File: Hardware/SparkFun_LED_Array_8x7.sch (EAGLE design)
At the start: 72 parts

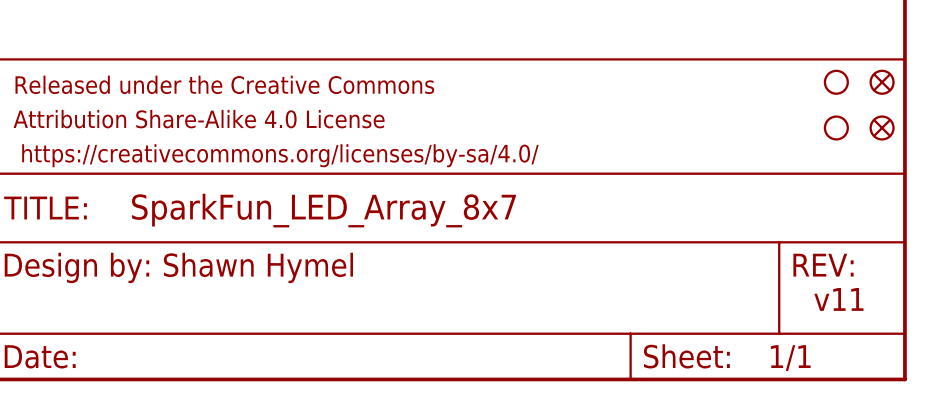
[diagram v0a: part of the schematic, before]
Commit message: Updated library to break up the page template and version number. Printed pdf of schematic.
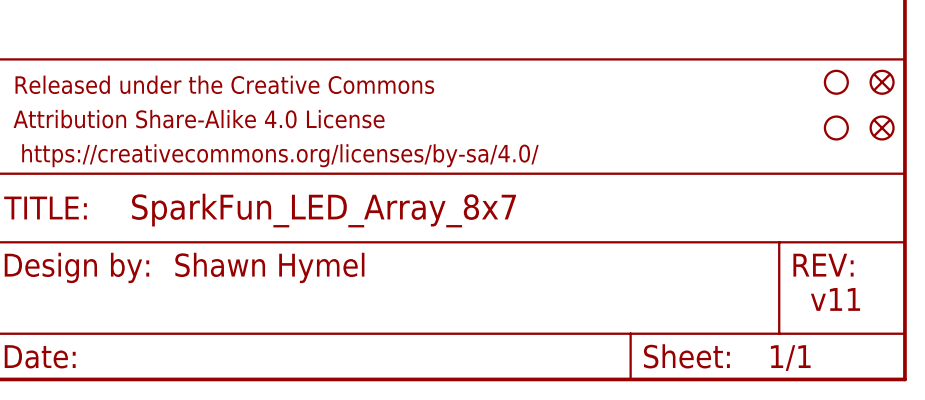
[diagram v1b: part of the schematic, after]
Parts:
- FRAME1: value (none) -> FRAME-LETTER; DESIGNER Shawn Hymel -> (none); VERSION v11 -> (none)
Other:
- note added: "Shawn Hymel"
- note added: "v11"
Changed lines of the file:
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@@
 <?xml version="1.0" encoding="utf-8"?>
 <!DOCTYPE eagle SYSTEM "eagle.dtd">
-<eagle version="7.3.0">
+<eagle version="7.2.0">
 <drawing>
 <settings>
@@
 <setting verticaltext="up"/>
 </settings>
-<grid distance="0.1" unitdist="inch" unit="inch" style="lines" multiple="1" display="no" altdistance="0.01" altunitdist="inch" altunit="inch"/>
+<grid distance="0.1" unitdist="inch" unit="inch" style="lines" multiple="1" display="yes" altdistance="0.01" altunitdist="inch" altunit="inch"/>
 <layers>
 <layer number="1" name="Top" color="4" fill="1" visible="no" active="no"/>
@@
 <layer number="112" name="tSilk" color="7" fill="1" visible="yes" active="yes"/>
 <layer number="113" name="IDFDebug" color="4" fill="1" visible="yes" active="yes"/>
+<layer number="114" name="Badge_Outline" color="7" fill="1" visible="yes" active="yes"/>
+<layer number="115" name="ReferenceISLANDS" color="7" fill="1" visible="yes" active="yes"/>
 <layer number="116" name="Patch_BOT" color="9" fill="4" visible="yes" active="yes"/>
+<layer number="118" name="Rect_Pads" color="7" fill="1" visible="yes" active="yes"/>
 <layer number="121" name="_tsilk" color="7" fill="1" visible="yes" active="yes"/>
 <layer number="122" name="_bsilk" color="7" fill="1" visible="yes" active="yes"/>
@@
 </classes>
 <parts>
-<part name="FRAME1" library="SparkFun-Aesthetics" deviceset="FRAME-LETTER" device="">
-<attribute name="DESIGNER" value="Shawn Hymel"/>
-<attribute name="VERSION" value="v11"/>
-</part>
+<part name="FRAME1" library="SparkFun-Aesthetics" deviceset="FRAME-LETTER" device=""/>
 <part name="R1" library="SparkFun-Resistors" deviceset="82OHM-1/10W-1%(0603)" device="SMD" value="82"/>
 <part name="D1" library="SparkFun-LED" deviceset="LED-RED" device="0603" value="RED"/>
@@
 <text x="24.638" y="119.38" size="1.778" layer="97" align="center">G</text>
 <text x="24.638" y="121.92" size="1.778" layer="97" align="center">H</text>
+<text x="167.64" y="12.7" size="2.54" layer="94" font="vector" align="center-left">Shawn Hymel</text>
+<text x="241.3" y="7.62" size="2.54" layer="94" font="vector" align="bottom-center">v11</text>
 </plain>
 <instances>
-<instance part="FRAME1" gate="G$1" x="0" y="0">
-<attribute name="DESIGNER" x="166.37" y="11.43" size="2.54" layer="94"/>
-<attribute name="VERSION" x="238.76" y="7.62" size="2.54" layer="94"/>
-</instance>
+<instance part="FRAME1" gate="G$1" x="0" y="0"/>
 <instance part="FRAME1" gate="V" x="147.32" y="0"/>
 <instance part="R1" gate="G$1" x="50.8" y="132.08" smashed="yes">
